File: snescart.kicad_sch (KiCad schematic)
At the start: 6 parts, among them P1 CASSETTE, U1 27C080

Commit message: expand
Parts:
- P1: footprint Library:CartEdge -> Library:ImperialCart
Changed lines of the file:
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@@
       (effects (font (size 1.27 1.27)))
     )
-    (property "Footprint" "Library:CartEdge" (at 113.03 141.605 0)
+    (property "Footprint" "Library:ImperialCart" (at 113.03 141.605 0)
       (effects (font (size 1.27 1.27)) hide)
     )

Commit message: cap
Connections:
- net GND: now also C3.1
- net VCC: now also C3.2
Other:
- moved on the sheet: C3
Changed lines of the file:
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@@
     )
   )
-  (symbol (lib_id "Device:C") (at 109.22 24.765 90) (unit 1)
-    (in_bom yes) (on_board yes) (dnp no) (fields_autoplaced)
-    (property "Reference" "C3" (at 108.585 21.59 0)
-      (effects (font (size 1.27 1.27)) (justify left))
-    )
-    (property "Value" "C" (at 111.125 21.59 0)
-      (effects (font (size 1.27 1.27)) (justify left))
-    )
-    (property "Footprint" "Library:Capacitor" (at 113.03 23.7998 0)
-      (effects (font (size 1.27 1.27)) hide)
-    )
-    (property "Datasheet" "~" (at 109.22 24.765 0)
+  (symbol (lib_id "Device:C") (at 93.98 23.495 90) (unit 1)
+    (in_bom yes) (on_board yes) (dnp no) (fields_autoplaced)
+    (property "Reference" "C3" (at 93.345 20.32 0)
+      (effects (font (size 1.27 1.27)) (justify left))
+    )
+    (property "Value" "C" (at 95.885 20.32 0)
+      (effects (font (size 1.27 1.27)) (justify left))
+    )
+    (property "Footprint" "Library:Capacitor" (at 97.79 22.5298 0)
+      (effects (font (size 1.27 1.27)) hide)
+    )
+    (property "Datasheet" "~" (at 93.98 23.495 0)
       (effects (font (size 1.27 1.27)) hide)
     )
@@
         )
       )
+    )
+  )
+  (symbol (lib_id "power:VCC") (at 97.79 23.495 270) (unit 1)
+    (in_bom yes) (on_board yes) (dnp no) (fields_autoplaced)
+    (property "Reference" "#PWR015" (at 93.98 23.495 0)
+      (effects (font (size 1.27 1.27)) hide)
+    )
+    (property "Value" "VCC" (at 101.6 24.13 90)
+      (effects (font (size 1.27 1.27)) (justify left))
+    )
+    (property "Footprint" "" (at 97.79 23.495 0)
+      (effects (font (size 1.27 1.27)) hide)
+    )
+    (property "Datasheet" "" (at 97.79 23.495 0)
+      (effects (font (size 1.27 1.27)) hide)
+    )
+    (pin "1")
+    (instances
+      (project "snescart"
+        (path "/066a4729-7396-4945-b543-8e17bff58a3f"
+          (reference "#PWR015") (unit 1)
+        )
+      )
+    )
+  )
+  (symbol (lib_id "power:GND") (at 90.17 23.495 270) (unit 1)
+    (in_bom yes) (on_board yes) (dnp no) (fields_autoplaced)
+    (property "Reference" "#PWR014" (at 83.82 23.495 0)
+      (effects (font (size 1.27 1.27)) hide)
+    )
+    (property "Value" "GND" (at 86.36 24.13 90)
+      (effects (font (size 1.27 1.27)) (justify right))
+    )
+    (property "Footprint" "" (at 90.17 23.495 0)
+      (effects (font (size 1.27 1.27)) hide)
+    )
+    (property "Datasheet" "" (at 90.17 23.495 0)
+      (effects (font (size 1.27 1.27)) hide)
+    )
+    (pin "1")
+    (instances
+      (project "snescart"
+        (path "/066a4729-7396-4945-b543-8e17bff58a3f"
+          (reference "#PWR014") (unit 1)
+        )
+      )

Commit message: redo
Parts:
- P1: footprint Library:ImperialCart -> Library:CartEdge
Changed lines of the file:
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@@
       (effects (font (size 1.27 1.27)))
     )
-    (property "Footprint" "Library:ImperialCart" (at 113.03 141.605 0)
+    (property "Footprint" "Library:CartEdge" (at 113.03 141.605 0)
       (effects (font (size 1.27 1.27)) hide)
     )

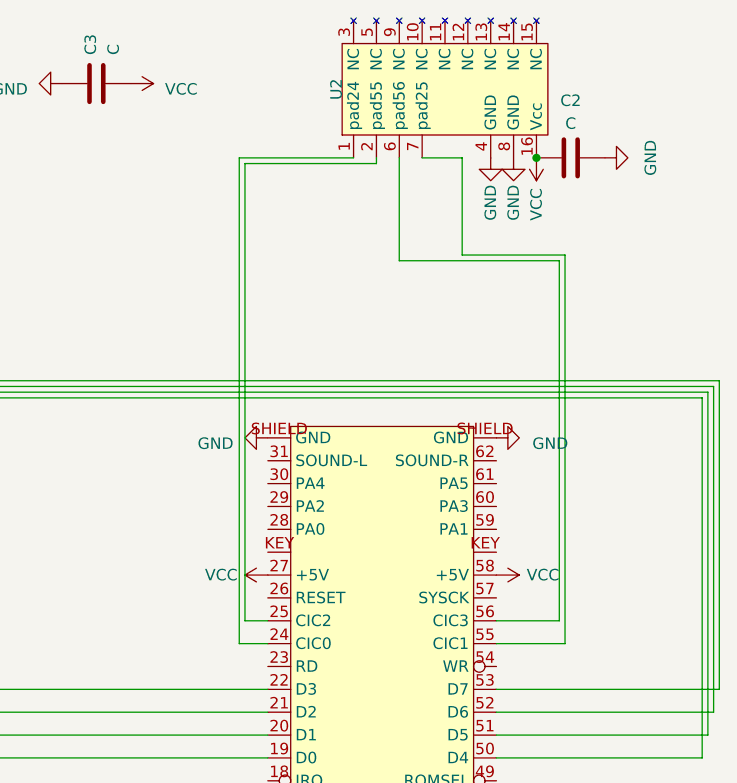
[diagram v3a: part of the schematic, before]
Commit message: swap cic pins
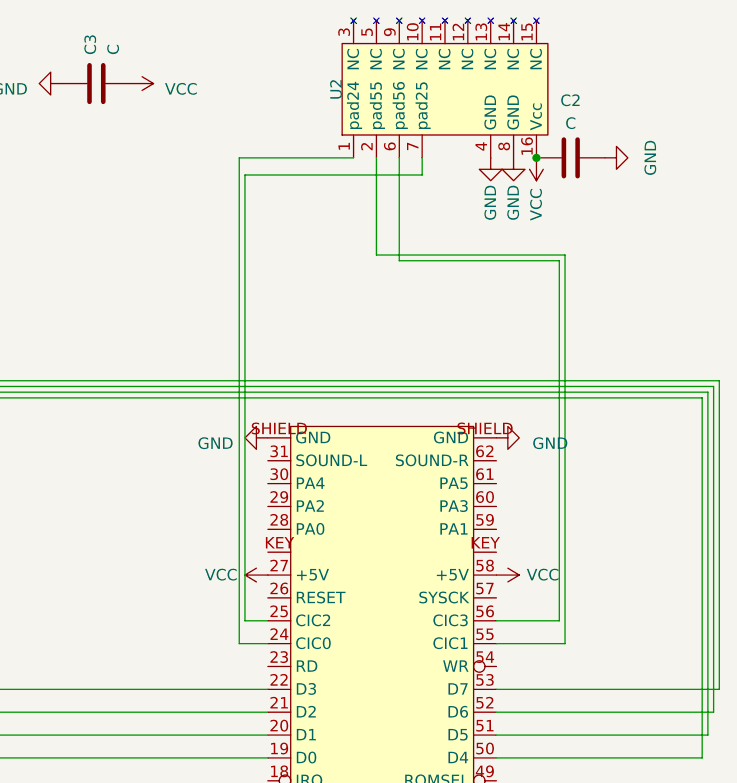
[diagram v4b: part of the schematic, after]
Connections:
- net at P1.25 (CIC2): now also U2.7 (pad25); no longer U2.2 (pad55)
- net at P1.55 (CIC1): now also U2.2 (pad55); no longer U2.7 (pad25)
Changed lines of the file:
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@@
     (stroke (width 0) (type default))
   )
-  (wire (pts (xy 125.095 32.385) (xy 125.095 31.75))
+  (wire (pts (xy 130.175 33.655) (xy 130.175 31.75))
     (stroke (width 0) (type default))
   )
@@
     (stroke (width 0) (type default))
   )
+  (wire (pts (xy 110.49 83.185) (xy 110.49 33.655))
+    (stroke (width 0) (type default))
+  )
   (wire (pts (xy 163.195 90.805) (xy 138.43 90.805))
     (stroke (width 0) (type default))
@@
     (stroke (width 0) (type default))
   )
-  (wire (pts (xy 130.175 31.75) (xy 134.62 31.75))
-    (stroke (width 0) (type default))
-  )
   (wire (pts (xy 57.785 90.805) (xy 113.03 90.805))
     (stroke (width 0) (type default))
@@
     (stroke (width 0) (type default))
   )
+  (wire (pts (xy 99.06 139.065) (xy 99.06 157.48))
+    (stroke (width 0) (type default))
+  )
+  (wire (pts (xy 138.43 98.425) (xy 161.29 98.425))
+    (stroke (width 0) (type default))
+  )
+  (wire (pts (xy 125.095 31.75) (xy 125.095 42.545))
+    (stroke (width 0) (type default))
+  )
+  (wire (pts (xy 162.56 57.15) (xy 162.56 93.345))
+    (stroke (width 0) (type default))
+  )
+  (wire (pts (xy 146.05 85.725) (xy 138.43 85.725))
+    (stroke (width 0) (type default))
+  )
+  (wire (pts (xy 59.69 96.52) (xy 77.47 96.52))
+    (stroke (width 0) (type default))
+  )
+  (wire (pts (xy 59.69 113.665) (xy 57.15 113.665))
+    (stroke (width 0) (type default))
+  )
+  (wire (pts (xy 155.575 131.445) (xy 138.43 131.445))
+    (stroke (width 0) (type default))
+  )
+  (wire (pts (xy 80.01 103.505) (xy 113.03 103.505))
+    (stroke (width 0) (type default))
+  )
+  (wire (pts (xy 80.01 144.145) (xy 97.79 144.145))
+    (stroke (width 0) (type default))
+  )
+  (wire (pts (xy 58.42 108.585) (xy 58.42 93.345))
+    (stroke (width 0) (type default))
+  )
+  (wire (pts (xy 110.49 33.655) (xy 130.175 33.655))
+    (stroke (width 0) (type default))
+  )
   (wire (pts (xy 113.03 83.185) (xy 110.49 83.185))
     (stroke (width 0) (type default))
   )
-  (wire (pts (xy 99.06 139.065) (xy 99.06 157.48))
-    (stroke (width 0) (type default))
-  )
-  (wire (pts (xy 138.43 98.425) (xy 161.29 98.425))
-    (stroke (width 0) (type default))
-  )
-  (wire (pts (xy 162.56 57.15) (xy 162.56 93.345))
-    (stroke (width 0) (type default))
-  )
-  (wire (pts (xy 146.05 85.725) (xy 138.43 85.725))
-    (stroke (width 0) (type default))
-  )
-  (wire (pts (xy 59.69 96.52) (xy 77.47 96.52))
-    (stroke (width 0) (type default))
-  )
-  (wire (pts (xy 59.69 113.665) (xy 57.15 113.665))
-    (stroke (width 0) (type default))
-  )
-  (wire (pts (xy 155.575 131.445) (xy 138.43 131.445))
-    (stroke (width 0) (type default))
-  )
-  (wire (pts (xy 80.01 103.505) (xy 113.03 103.505))
-    (stroke (width 0) (type default))
-  )
-  (wire (pts (xy 80.01 144.145) (xy 97.79 144.145))
-    (stroke (width 0) (type default))
-  )
-  (wire (pts (xy 58.42 108.585) (xy 58.42 93.345))
-    (stroke (width 0) (type default))
-  )
   (wire (pts (xy 161.925 57.785) (xy 161.925 95.885))
     (stroke (width 0) (type default))
@@
     (stroke (width 0) (type default))
   )
-  (wire (pts (xy 110.49 32.385) (xy 125.095 32.385))
-    (stroke (width 0) (type default))
-  )
   (wire (pts (xy 80.01 149.225) (xy 96.52 149.225))
     (stroke (width 0) (type default))
@@
     (stroke (width 0) (type default))
   )
-  (wire (pts (xy 134.62 42.545) (xy 146.05 42.545))
-    (stroke (width 0) (type default))
-  )
   (wire (pts (xy 157.48 158.75) (xy 157.48 123.825))
     (stroke (width 0) (type default))
@@
     (stroke (width 0) (type default))
   )
+  (wire (pts (xy 125.095 42.545) (xy 146.05 42.545))
+    (stroke (width 0) (type default))
+  )
   (wire (pts (xy 80.01 136.525) (xy 99.695 136.525))
     (stroke (width 0) (type default))
@@
     (stroke (width 0) (type default))
   )
-  (wire (pts (xy 134.62 31.75) (xy 134.62 42.545))
-    (stroke (width 0) (type default))
-  )
   (wire (pts (xy 80.01 126.365) (xy 113.03 126.365))
     (stroke (width 0) (type default))
@@
     (stroke (width 0) (type default))
   )
-  (wire (pts (xy 110.49 83.185) (xy 110.49 32.385))
-    (stroke (width 0) (type default))
-  )
